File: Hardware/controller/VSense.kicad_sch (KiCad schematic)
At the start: 16 parts, among them J501 Conn_01x04, U501 OPA277

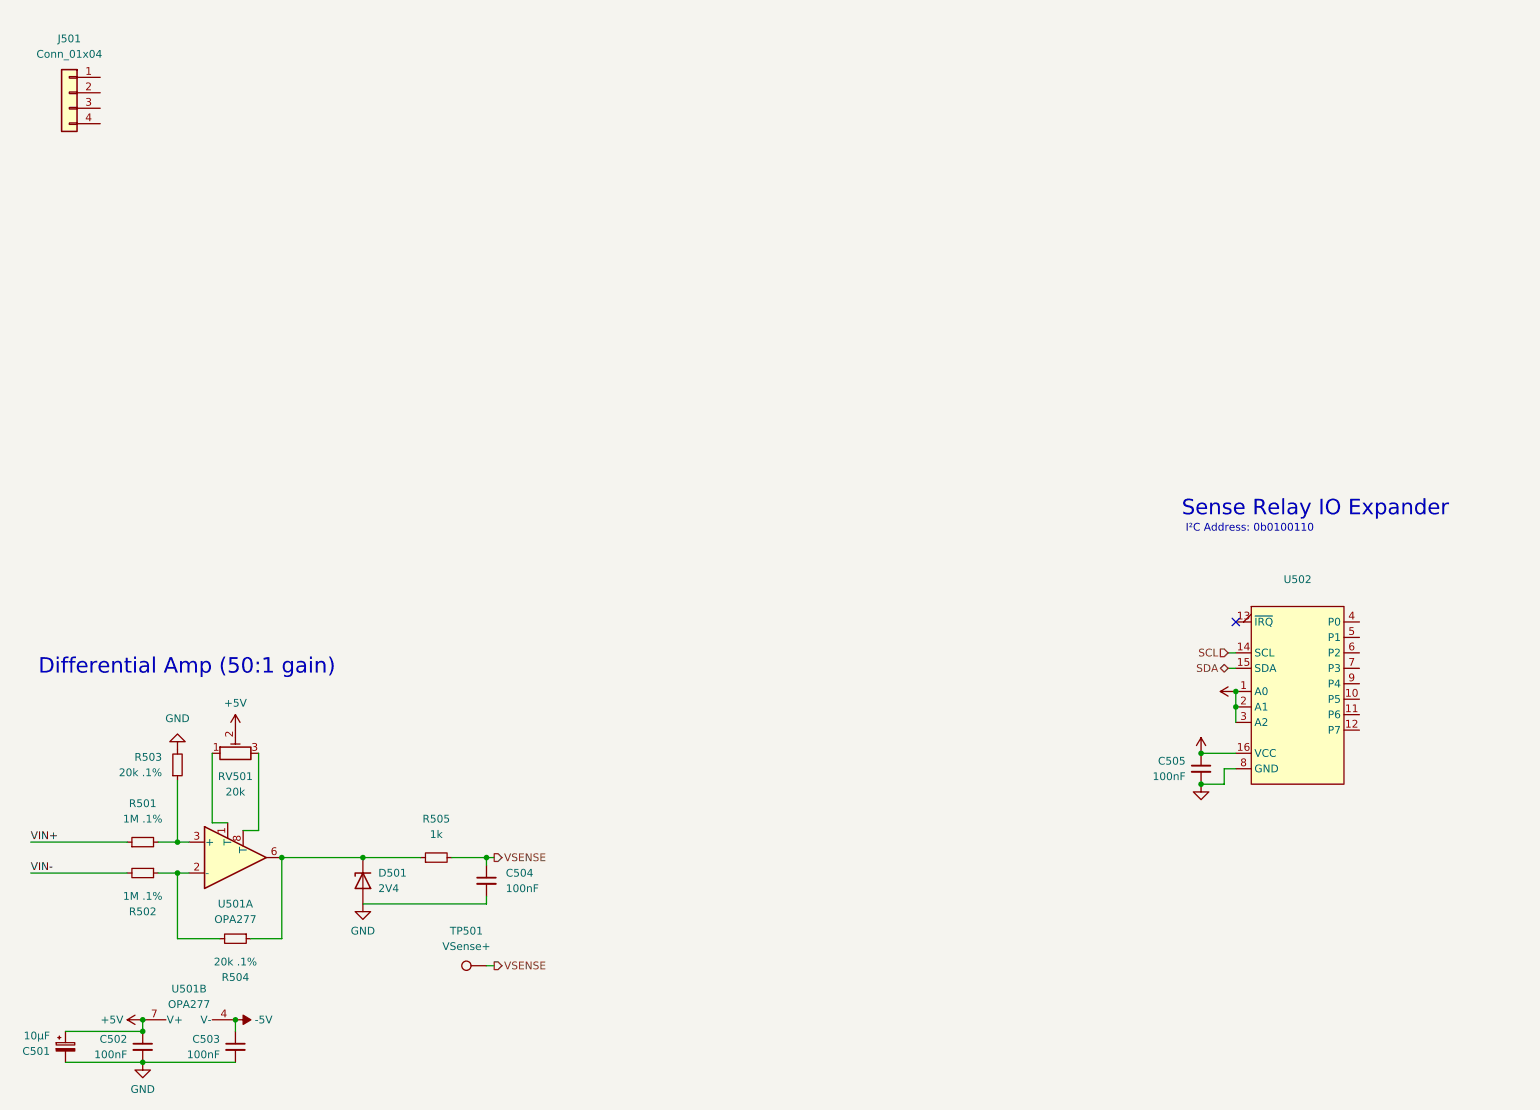
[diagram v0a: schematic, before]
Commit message: Work on controller VSense, power
- Routed 3V3 switching supply

- Created footprint and symbols for Kemet EA2 series latching relay

- Added relays to controller to handle routing of voltage sense inputs
  to the sampling ADC
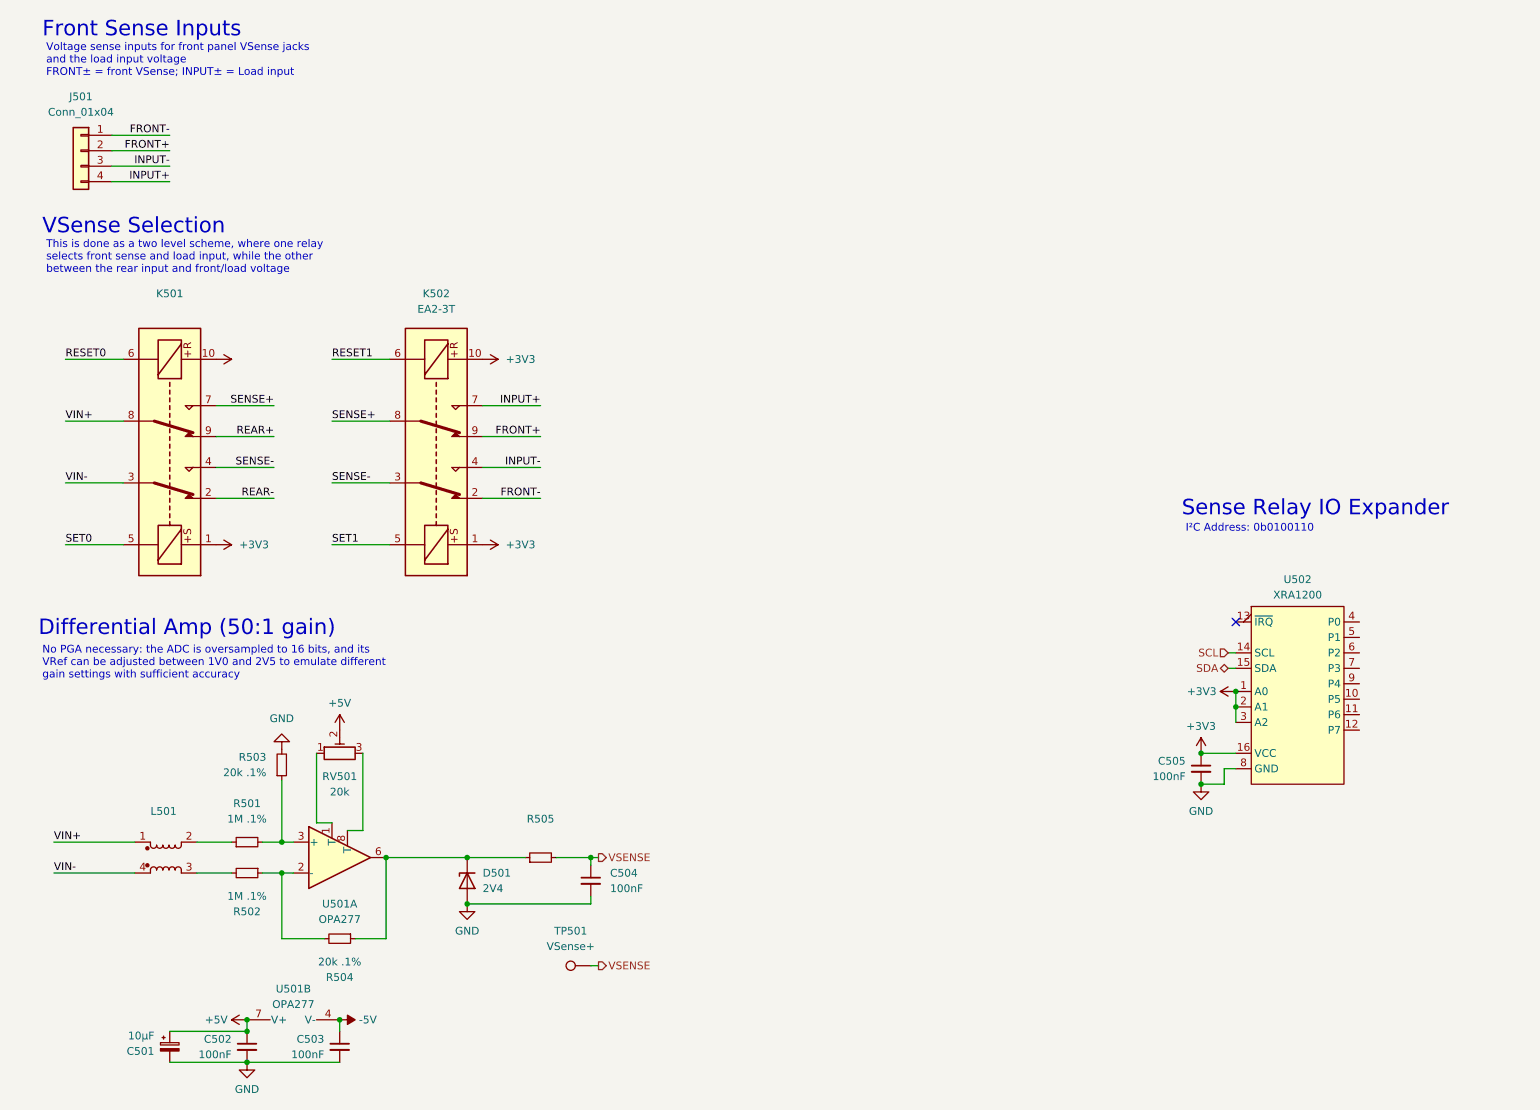
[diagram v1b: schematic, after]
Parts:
- added K501: (no value), symbol programmable-load:EA2-3T
- added K502: EA2-3T, programmable-load:KEMET-EA2, symbol programmable-load:EA2-3T
- added L501: (no value), symbol Device:L_Coupled_1243
- R505: value 1k -> (none)
- U502: value (none) -> XRA1200; footprint (none) -> Package_SO:TSSOP-16_4.4x5mm_P0.65mm
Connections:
- net +3V3: now also K501.1, K501.10, K502.1, K502.10
- net VIN+: now also K501.8, L501.1; no longer R501.1
- net VIN-: now also K501.3, L501.4; no longer R502.2
- net FRONT-: now reaches J501.1 (Pin_1)
- net FRONT-: now also K502.2
- net FRONT+: now reaches J501.2 (Pin_2)
- net FRONT+: now also K502.9
- net INPUT-: now reaches J501.3 (Pin_3)
- net INPUT-: now also K502.4
- net INPUT+: now reaches J501.4 (Pin_4)
- net INPUT+: now also K502.7
- new net: L501.2, R501.1
- new net: L501.3, R502.2
- new net REAR+: K501.9
- new net REAR-: K501.2
- new net RESET0: K501.6
- new net RESET1: K502.6
- new net SENSE+: K501.7, K502.8
- new net SENSE-: K501.4, K502.3
- new net SET0: K501.5
- new net SET1: K502.5
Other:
- note added: "Front Sense Inputs"
- note added: "No PGA necessary: the ADC is oversampled to 16 bits, and its VRef can be adjusted between 1V0 and 2V5 to emulate different gain settings with sufficient accuracy"
- note added: "This is done as a two level scheme, where one relay selects front sense and load input, while the other between the rear input and front/load voltage"
- note added: "VSense Selection"
- note added: "Voltage sense inputs for front panel VSense jacks and the load input voltage FRONT± = front VSense; INPUT± = Load input"
- moved on the sheet: C501, C502, C503, C504, D501, J501, R501, R502, R503, R504, R505, RV501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

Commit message: More work on new controller board
- Switched mains connection for a push-in screw terminal, rather than a
  pluggable block (takes up less space, less parts)

- Added input terminal for rear VSense inputs

- Added -5V supply (same circuit as on analog board; required for
  voltage input sense)

- Replaced beeper with a side-firing version. It takes up a bunch less
  space vertically, and also now added a resistor to (hopefully) make it
  somewhat more quiet

- Added connector for bonus displays
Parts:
- added D502, D503, D504, D505: SM4007, Diode_SMD:D_SMA_Handsoldering, symbol Diode:SM4007
- added J502: Conn_01x02, programmable-load:CUI_TBLH10-350-02BK, symbol Connector_Generic:Conn_01x02
- added Q501, Q502, Q503, Q504: MMBT3904, Package_TO_SOT_SMD:SOT-323_SC-70_Handsoldering, symbol Transistor_BJT:MMBT3904
- added R506, R507, R508, R509: 10k, Resistor_SMD:R_0805_2012Metric_Pad1.20x1.40mm_HandSolder, symbol Device:R_Small
- K501: value (none) -> EA2-3T; footprint (none) -> programmable-load:KEMET-EA2
- L501: value (none) -> DR331-513BE; footprint (none) -> programmable-load:Bourns-DR331-0-0-MFG; symbol Device:L_Coupled_1243 -> Device:L_Ferrite_Coupled_1423; MPN ACM-21-670M-T -> DR331-513BE
- R505: value (none) -> 1k; footprint (none) -> Resistor_SMD:R_0805_2012Metric_Pad1.20x1.40mm_HandSolder
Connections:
- net +3V3: now also C501.1, D502.1 (K), D503.1 (K), D504.1 (K), D505.1 (K)
- net +5V: no longer C501.1
- net FRONT+: now also J501.1 (Pin_1), K502.2; no longer J501.2 (Pin_2), K502.9
- net FRONT-: now also J501.2 (Pin_2), K502.9; no longer J501.1 (Pin_1), K502.2
- net GND: now also Q501.2 (E), Q502.2 (E), Q503.2 (E), Q504.2 (E), R506.1, R507.1, R508.1, R509.1
- net INPUT+: now also J501.3 (Pin_3), K502.4; no longer J501.4 (Pin_4), K502.7
- net INPUT-: now also J501.4 (Pin_4), K502.7; no longer J501.3 (Pin_3), K502.4
- net REAR+: now also K501.2, J502.1 (Pin_1); no longer K501.9
- net REAR-: now also K501.9, J502.2 (Pin_2); no longer K501.2
- net RESET0: now also D503.2 (A), Q501.3 (C)
- net RESET1: now also D505.2 (A), Q504.3 (C)
- net SENSE+: now also K501.4, K502.3; no longer K501.7, K502.8
- net SENSE-: now also K501.7, K502.8; no longer K501.4, K502.3
- net SET0: now also D502.2 (A), Q502.3 (C)
- net SET1: now also D504.2 (A), Q503.3 (C)
- net VIN+: now also K501.3, L501.2; no longer K501.8, L501.1
- net VIN-: now also K501.8, L501.1; no longer K501.3, L501.4
- net RELAY_RESET0: now reaches U502.4 (P0)
- net RELAY_RESET0: now also Q501.1 (B), R507.2
- net RELAY_SET0: now reaches U502.5 (P1)
- net RELAY_SET0: now also Q502.1 (B), R506.2
- net RELAY_RESET1: now reaches U502.6 (P2)
- net RELAY_RESET1: now also Q504.1 (B), R509.2
- net RELAY_SET1: now reaches U502.7 (P3)
- net RELAY_SET1: now also Q503.1 (B), R508.2
- net at R501.1: now also L501.3; no longer L501.2
- net at R502.2: now also L501.4; no longer L501.3
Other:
- note added: "Relay Drivers"
- moved on the sheet: K502

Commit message: Work on layout analog board
- Moved the heatsink to be horizontal near the bottom of the analog
  board, to give more open space for the analog circuitry away from the
  hot MOSFETs

- Minor tweak to bonus display (cutout for front panel jacks)
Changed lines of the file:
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@@
+    (stroke (width 0) (type default) (color 0 0 0 0))
+  )
+  (wire (pts (xy 64.77 135.89) (xy 61.595 135.89))
     (stroke (width 0) (type default) (color 0 0 0 0))
   )
@@
     (stroke (width 0) (type default) (color 0 0 0 0))
   )
+  (wire (pts (xy 64.77 138.43) (xy 64.77 135.89))
+    (stroke (width 0) (type default) (color 0 0 0 0))
+  )
   (wire (pts (xy 218.44 130.175) (xy 218.44 132.715))
     (stroke (width 0) (type default) (color 0 0 0 0))
@@
   )
   (wire (pts (xy 67.31 149.225) (xy 67.31 137.795))
+    (stroke (width 0) (type default) (color 0 0 0 0))
+  )
+  (wire (pts (xy 61.595 135.89) (xy 61.595 137.16))
     (stroke (width 0) (type default) (color 0 0 0 0))
   )
@@
     (pin "9")
   )
-  (symbol (lib_id "power:GND") (at 61.595 137.16 180) (unit 1)
-    (in_bom yes) (on_board yes) (fields_autoplaced)
-    (property "Reference" "#PWR0503" (id 0) (at 61.595 130.81 0)
-      (effects (font (size 1.27 1.27)) hide)
-    )
-    (property "Value" "GND" (id 1) (at 61.595 132.08 0))
-    (property "Footprint" "" (id 2) (at 61.595 137.16 0)
-      (effects (font (size 1.27 1.27)) hide)
-    )
-    (property "Datasheet" "" (id 3) (at 61.595 137.16 0)
-      (effects (font (size 1.27 1.27)) hide)
-    )
+  (symbol (lib_id "power:GND") (at 64.77 138.43 0) (unit 1)
+    (in_bom yes) (on_board yes) (fields_autoplaced)
+    (property "Reference" "#PWR0503" (id 0) (at 64.77 144.78 0)
+      (effects (font (size 1.27 1.27)) hide)
+    )
+    (property "Value" "GND" (id 1) (at 64.77 143.51 0))
+    (property "Footprint" "" (id 2) (at 64.77 138.43 0)
+      (effects (font (size 1.27 1.27)) hide)
+    )
+    (property "Datasheet" "" (id 3) (at 64.77 138.43 0)
+      (effects (font (size 1.27 1.27)) hide)
+    )

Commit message: Begin cleaning up controller for rework
- Removed some of the old stuff

- Added USB host connector for front panel (including footprint for new
  ESD boi)
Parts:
- U: renamed from R506; value 10k -> (none); footprint Resistor_SMD:R_0805_2012Metric_Pad1.20x1.40mm_HandSolder -> (none)
- U: renamed from U501; value OPA277 -> (none); footprint Package_SO:SOIC-8_3.9x4.9mm_P1.27mm -> (none)
- U: renamed from R505; value 1k -> (none); footprint Resistor_SMD:R_0805_2012Metric_Pad1.20x1.40mm_HandSolder -> (none)
- U: renamed from R508; value 10k -> (none); footprint Resistor_SMD:R_0805_2012Metric_Pad1.20x1.40mm_HandSolder -> (none)
- U: renamed from D501; value 2V4 -> (none); footprint Diode_SMD:D_MiniMELF_Handsoldering -> (none)
- U: renamed from R504; value 20k .1% -> (none); footprint Resistor_SMD:R_0805_2012Metric_Pad1.20x1.40mm_HandSolder -> (none)
- U: renamed from C501; value 10µF -> (none); footprint Capacitor_Tantalum_SMD:CP_EIA-3216-18_Kemet-A_Pad1.58x1.35mm_HandSolder -> (none)
- U: renamed from U502; value XRA1200 -> (none); footprint Package_SO:TSSOP-16_4.4x5mm_P0.65mm -> (none)
- U: renamed from R509; value 10k -> (none); footprint Resistor_SMD:R_0805_2012Metric_Pad1.20x1.40mm_HandSolder -> (none)
- U: renamed from K501; value EA2-3T -> (none); footprint programmable-load:KEMET-EA2 -> (none)
- U: renamed from L501; value DR331-513BE -> (none); footprint programmable-load:Bourns-DR331-0-0-MFG -> (none)
- U: renamed from TP501; value VSense+ -> (none); footprint TestPoint:TestPoint_Keystone_5000-5004_Miniature -> (none)
- U: renamed from Q501; value MMBT3904 -> (none); footprint Package_TO_SOT_SMD:SOT-323_SC-70_Handsoldering -> (none)
- U: renamed from R502; value 1M .1% -> (none); footprint Resistor_SMD:R_0805_2012Metric_Pad1.20x1.40mm_HandSolder -> (none)
- U: renamed from C505; value 100nF -> (none); footprint Capacitor_SMD:C_0805_2012Metric_Pad1.18x1.45mm_HandSolder -> (none)
- U: renamed from R501; value 1M .1% -> (none); footprint Resistor_SMD:R_0805_2012Metric_Pad1.20x1.40mm_HandSolder -> (none)
- U: renamed from C503; value 100nF -> (none); footprint Capacitor_SMD:C_0805_2012Metric_Pad1.18x1.45mm_HandSolder -> (none)
- U: renamed from D503; value SM4007 -> (none); footprint Diode_SMD:D_SMA_Handsoldering -> (none)
- U: renamed from K502; value EA2-3T -> (none); footprint programmable-load:KEMET-EA2 -> (none)
- U: renamed from D504; value SM4007 -> (none); footprint Diode_SMD:D_SMA_Handsoldering -> (none)
- U: renamed from R503; value 20k .1% -> (none); footprint Resistor_SMD:R_0805_2012Metric_Pad1.20x1.40mm_HandSolder -> (none)
- U: renamed from D502; value SM4007 -> (none); footprint Diode_SMD:D_SMA_Handsoldering -> (none)
- U: renamed from J502; value Conn_01x02 -> (none); footprint programmable-load:CUI_TBLH10-350-02BK -> (none)
- U: renamed from Q503; value MMBT3904 -> (none); footprint Package_TO_SOT_SMD:SOT-323_SC-70_Handsoldering -> (none)
- U: renamed from C504; value 100nF -> (none); footprint Capacitor_SMD:C_0805_2012Metric_Pad1.18x1.45mm_HandSolder -> (none)
- U: renamed from Q502; value MMBT3904 -> (none); footprint Package_TO_SOT_SMD:SOT-323_SC-70_Handsoldering -> (none)
- U: renamed from R507; value 10k -> (none); footprint Resistor_SMD:R_0805_2012Metric_Pad1.20x1.40mm_HandSolder -> (none)
- U: renamed from C502; value 100nF -> (none); footprint Capacitor_SMD:C_0805_2012Metric_Pad1.18x1.45mm_HandSolder -> (none)
- U: renamed from RV501; value 20k -> (none); footprint programmable-load:Potentiometer_Nidec_Copal_CT94EY -> (none)
- U: renamed from Q504; value MMBT3904 -> (none); footprint Package_TO_SOT_SMD:SOT-323_SC-70_Handsoldering -> (none)
- U: renamed from J501; value Conn_01x04 -> (none); footprint programmable-load:CUI_TBLH10-350-04BK -> (none)
- U: renamed from D505; value SM4007 -> (none); footprint Diode_SMD:D_SMA_Handsoldering -> (none)
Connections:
- net +5V: no longer U.7 (V+)
- net -5V: no longer U.4 (V-)
